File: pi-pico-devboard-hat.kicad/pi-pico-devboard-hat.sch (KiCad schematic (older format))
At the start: 12 parts, among them J1 Conn_01x24_Male, J2 Conn_Pico_1, J3 Conn_SWD, J4 Conn_Pico_2, P1 Conn_02x20_Odd_Even, SW1 SW_Reset, U1 Pico

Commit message: added footprints
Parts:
- D1: footprint (none) -> Diode_THT:D_DO-41_SOD81_P7.62mm_Horizontal
- J2, J4: footprint (none) -> Connector_PinHeader_2.54mm:PinHeader_1x20_P2.54mm_Vertical
- J3: footprint (none) -> Connector_PinHeader_2.54mm:PinHeader_1x03_P2.54mm_Vertical
- SW1: footprint (none) -> Button_Switch_THT:SW_PUSH_6mm
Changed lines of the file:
@@
 F 0 "J2" H 6400 5500 50  0000 C CNN
 F 1 "Conn_Pico_1" H 6400 5350 50  0000 C CNN
-F 2 "" H 6300 4300 50  0001 C CNN
+F 2 "Connector_PinHeader_2.54mm:PinHeader_1x20_P2.54mm_Vertical" H 6300 4300 50  0001 C CNN
 F 3 "~" H 6300 4300 50  0001 C CNN
 	1    6300 4300
@@
 F 0 "J4" H 9050 3050 50  0000 C CNN
 F 1 "Conn_Pico_2" H 9050 3200 50  0000 C CNN
-F 2 "" H 8900 4400 50  0001 C CNN
+F 2 "Connector_PinHeader_2.54mm:PinHeader_1x20_P2.54mm_Vertical" H 8900 4400 50  0001 C CNN
 F 3 "~" H 8900 4400 50  0001 C CNN
 	1    8900 4400
@@
 F 0 "J3" V 7754 6062 50  0000 R CNN
 F 1 "Conn_SWD" V 7663 6062 50  0000 R CNN
-F 2 "" H 7600 6250 50  0001 C CNN
+F 2 "Connector_PinHeader_2.54mm:PinHeader_1x03_P2.54mm_Vertical" H 7600 6250 50  0001 C CNN
 F 3 "~" H 7600 6250 50  0001 C CNN
 	1    7600 6250
@@
 F 0 "SW1" H 9400 4685 50  0000 C CNN
 F 1 "SW_Reset" H 9400 4594 50  0000 C CNN
-F 2 "" H 9400 4600 50  0001 C CNN
+F 2 "Button_Switch_THT:SW_PUSH_6mm" H 9400 4600 50  0001 C CNN
 F 3 "~" H 9400 4600 50  0001 C CNN
 	1    9400 4400
@@
 F 0 "D1" V 9846 2870 50  0000 R CNN
 F 1 "D_Schottky" V 9755 2870 50  0000 R CNN
-F 2 "" H 9800 2950 50  0001 C CNN
+F 2 "Diode_THT:D_DO-41_SOD81_P7.62mm_Horizontal" H 9800 2950 50  0001 C CNN
 F 3 "~" H 9800 2950 50  0001 C CNN
 	1    9800 2950

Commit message: updated footprint for pico
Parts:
- U1: footprint RPi_Pico:RPi_Pico_SMD_TH -> user:RPi_Pico_SMD_TH
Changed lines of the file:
@@
 F 0 "U1" H 7600 5565 50  0000 C CNN
 F 1 "Pico" H 7600 5474 50  0000 C CNN
-F 2 "RPi_Pico:RPi_Pico_SMD_TH" V 7600 4350 50  0001 C CNN
+F 2 "user:RPi_Pico_SMD_TH" V 7600 4350 50  0001 C CNN
 F 3 "" H 7600 4350 50  0001 C CNN
 	1    7600 4350

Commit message: Rev 2: removed unneeded connectors
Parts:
- removed J2: Conn_Pico_1, Connector_PinHeader_2.54mm:PinHeader_1x20_P2.54mm_Vertical, symbol Connector:Conn_01x20_Male
- removed J3: Conn_SWD, Connector_PinHeader_2.54mm:PinHeader_1x03_P2.54mm_Vertical, symbol Connector:Conn_01x03_Male
- removed J4: Conn_Pico_2, Connector_PinHeader_2.54mm:PinHeader_1x20_P2.54mm_Vertical, symbol Connector:Conn_01x20_Male
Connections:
- wire segments 147 -> 135
- no-connect marks 4 -> 28
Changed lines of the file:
@@
 Sheet 1 1
 Title "pi-pico-devboard-hat"
-Date "2021-03-11"
-Rev "1"
+Date "2021-03-18"
+Rev "2"
 Comp "Bernhard Bablok"
 Comment1 "https://github.com/bablokb/pi-pico-devboard-hat"
@@
 $EndComp
 $Comp
-L Connector:Conn_01x20_Male J2
-U 1 1 604A53BA
-P 6300 4300
-F 0 "J2" H 6400 5500 50  0000 C CNN
-F 1 "Conn_Pico_1" H 6400 5350 50  0000 C CNN
-F 2 "Connector_PinHeader_2.54mm:PinHeader_1x20_P2.54mm_Vertical" H 6300 4300 50  0001 C CNN
-F 3 "~" H 6300 4300 50  0001 C CNN
-	1    6300 4300
-	1    0    0    -1
-$EndComp
-$Comp
-L Connector:Conn_01x20_Male J4
-U 1 1 604AF8E6
-P 8900 4400
-F 0 "J4" H 9050 3050 50  0000 C CNN
-F 1 "Conn_Pico_2" H 9050 3200 50  0000 C CNN
-F 2 "Connector_PinHeader_2.54mm:PinHeader_1x20_P2.54mm_Vertical" H 8900 4400 50  0001 C CNN
-F 3 "~" H 8900 4400 50  0001 C CNN
-	1    8900 4400
-	-1   0    0    1
-$EndComp
-$Comp
-L Connector:Conn_01x03_Male J3
-U 1 1 604B1D35
-P 7600 6250
-F 0 "J3" V 7754 6062 50  0000 R CNN
-F 1 "Conn_SWD" V 7663 6062 50  0000 R CNN
-F 2 "Connector_PinHeader_2.54mm:PinHeader_1x03_P2.54mm_Vertical" H 7600 6250 50  0001 C CNN
-F 3 "~" H 7600 6250 50  0001 C CNN
-	1    7600 6250
-	0    -1   -1   0
-$EndComp
-$Comp
 L Switch:SW_Push SW1
 U 1 1 604B3ACB
@@
 $EndComp
 Wire Wire Line
-	8300 3500 8700 3500
-Wire Wire Line
-	8300 3600 8700 3600
-Wire Wire Line
-	8300 3700 8700 3700
-Wire Wire Line
-	8300 3800 8700 3800
-Wire Wire Line
-	8300 3900 8700 3900
-Wire Wire Line
 	8300 4000 8700 4000
 Wire Wire Line
-	8300 4100 8700 4100
-Wire Wire Line
 	8300 4200 8700 4200
 Wire Wire Line
 	8300 4300 8700 4300
 Wire Wire Line
-	8300 4400 8700 4400
-Wire Wire Line
 	8300 4500 8700 4500
 Wire Wire Line
-	8300 4600 8700 4600
-Wire Wire Line
 	8300 4700 8700 4700
 Wire Wire Line
@@
 	8300 5000 8700 5000
 Wire Wire Line
-	8300 5100 8700 5100
-Wire Wire Line
 	8300 5200 8700 5200
 Wire Wire Line
 	8300 5300 8700 5300
 Wire Wire Line
-	6500 3400 6850 3400
-Wire Wire Line
-	6500 3500 6750 3500
-Wire Wire Line
-	6500 3600 6900 3600
-Wire Wire Line
 	6500 3700 6900 3700
 Wire Wire Line
@@
 	6500 4000 6900 4000
 Wire Wire Line
-	6500 4100 6900 4100
-Wire Wire Line
 	6500 4200 6900 4200
 Wire Wire Line
@@
 Wire Wire Line
 	6500 4500 6900 4500
-Wire Wire Line
-	6500 4600 6900 4600
-Wire Wire Line
-	6500 4700 6900 4700
-Wire Wire Line
-	6500 4800 6900 4800
-Wire Wire Line
-	6500 4900 6900 4900
-Wire Wire Line
-	6500 5000 6900 5000
-Wire Wire Line
-	6500 5100 6900 5100
-Wire Wire Line
-	6500 5200 6900 5200
-Wire Wire Line
-	6500 5300 6900 5300
-Wire Wire Line
-	8700 4400 9200 4400
-Connection ~ 8700 4400
 $Comp
 L power:GND #PWR07
@@
 	9600 4400 9800 4400
 Wire Wire Line
-	8700 3600 9800 3600
-Wire Wire Line
 	9800 3600 9800 4400
-Connection ~ 8700 3600
 Wire Wire Line
 	9800 4600 9800 4400
-Connection ~ 8700 4600
 Connection ~ 9800 4400
 Connection ~ 9800 4600
 Wire Wire Line
-	8700 4600 9800 4600
-Wire Wire Line
 	9800 4600 9800 5100
-Wire Wire Line
-	9800 5100 8700 5100
-Connection ~ 8700 5100
 $Comp
 L power:GND #PWR05
@@
 $EndComp
 Wire Wire Line
-	6500 3600 5950 3600
-Wire Wire Line
 	5950 3600 5950 4100
-Connection ~ 6500 3600
 Connection ~ 5950 4100
 Wire Wire Line
@@
 Wire Wire Line
 	5950 4100 5950 4600
-Wire Wire Line
-	5950 4600 6500 4600
-Connection ~ 6500 4600
-Wire Wire Line
-	6500 5100 5950 5100
-Connection ~ 6500 5100
 Connection ~ 5950 4600
 $Comp
@@
 	0    -1   -1   0
 $EndComp
-Connection ~ 8700 3500
 $Comp
 L power:PWR_FLAG #FLG0101
@@
 	7600 5650 7600 5500
 Connection ~ 9800 5100
-Wire Wire Line
-	6500 4100 5950 4100
-Connection ~ 6500 4100
 NoConn ~ 2400 2400
 NoConn ~ 2900 2400
@@
 $EndComp
 Connection ~ 2200 950
-Wire Wire Line
-	8300 3400 8700 3400
 Text Label 10300 3400 2    50   ~ 0
 VBUS
@@
 Wire Wire Line
 	10300 3400 10500 3400
-Text Label 8350 3400 0    50   ~ 0
-VBUS
 Text Label 10300 3700 2    50   ~ 0
 3V3_EN
@@
 Wire Wire Line
 	9800 3100 9800 3500
-Wire Wire Line
-	8700 3500 9800 3500
 Text Label 10300 3500 2    50   ~ 0
 VSYS
@@
 Text Label 7700 5900 0    50   ~ 0
 GPIO24(GEN5)
-Wire Wire Line
-	7700 5500 7700 6050
-Wire Wire Line
-	7600 5650 7600 6050
 Text Label 7500 5900 2    50   ~ 0
 GPIO25(GEN6)
-Wire Wire Line
-	7500 5500 7500 6050
 Text Label 6850 3100 0    50   ~ 0
 GPIO15(RXD0)
@@
 Wire Wire Line
 	6850 3100 6850 3400
-Connection ~ 6850 3400
 Wire Wire Line
 	6850 3400 6900 3400
 Wire Wire Line
 	6750 3000 6750 3500
-Connection ~ 6750 3500
 Wire Wire Line
 	6750 3500 6900 3500
+Wire Wire Line
+	5950 4600 6900 4600
+Wire Wire Line
+	5950 5100 6900 5100
+Wire Wire Line
+	5950 3600 6900 3600
+Wire Wire Line
+	5950 4100 6900 4100
+Wire Wire Line
+	6500 4700 6900 4700
+Wire Wire Line
+	6500 4800 6900 4800
+Wire Wire Line
+	6500 4900 6900 4900
+Wire Wire Line
+	6500 5000 6900 5000
+Wire Wire Line
+	6500 5200 6900 5200
+Wire Wire Line
+	6500 5300 6900 5300
+Wire Wire Line
+	8300 4400 9200 4400
+Wire Wire Line
+	8300 3600 9800 3600
+Wire Wire Line
+	8300 3500 9800 3500
+Wire Wire Line
+	8300 5100 9800 5100
+Wire Wire Line
+	8300 4600 9800 4600
+Text Label 8350 3400 0    50   ~ 0
+VBUS
+Wire Wire Line
+	8300 3400 8350 3400
+Wire Wire Line
+	8300 3700 8350 3700
+Wire Wire Line
+	8300 3800 8350 3800
+Wire Wire Line
+	8300 3900 8350 3900
+Wire Wire Line
+	8300 4100 8350 4100
+NoConn ~ 6500 3700
+NoConn ~ 6500 3800
+NoConn ~ 6500 3900
+NoConn ~ 6500 4000
+NoConn ~ 6500 4200
+NoConn ~ 6500 4300
+NoConn ~ 6500 4400
+NoConn ~ 6500 4500
+NoConn ~ 6500 4700
+NoConn ~ 6500 4800
+NoConn ~ 6500 4900
+NoConn ~ 6500 5000
+NoConn ~ 6500 5200
+NoConn ~ 6500 5300
+NoConn ~ 8700 4000
+NoConn ~ 8700 4200
+NoConn ~ 8700 4300
+NoConn ~ 8700 4500
+NoConn ~ 8700 4700
+NoConn ~ 8700 4800
+NoConn ~ 8700 4900
+NoConn ~ 8700 5000
+NoConn ~ 8700 5200
+NoConn ~ 8700 5300
+Wire Wire Line
+	7700 5500 7700 5900
+Wire Wire Line
+	7500 5500 7500 5900
 $EndSCHEMATC

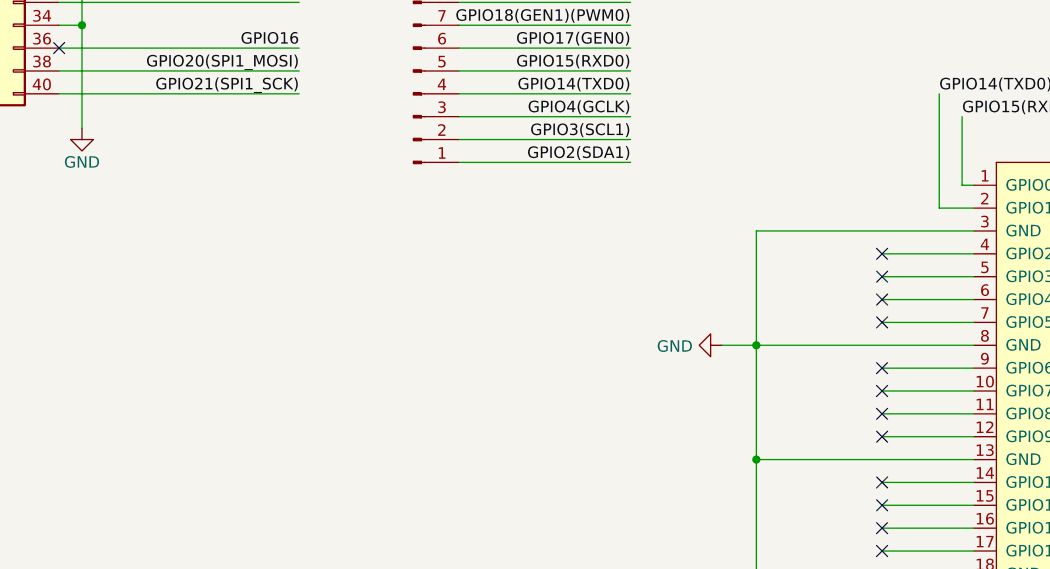
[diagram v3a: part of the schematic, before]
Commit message: Rev 3: added IC-connector with optional pullups
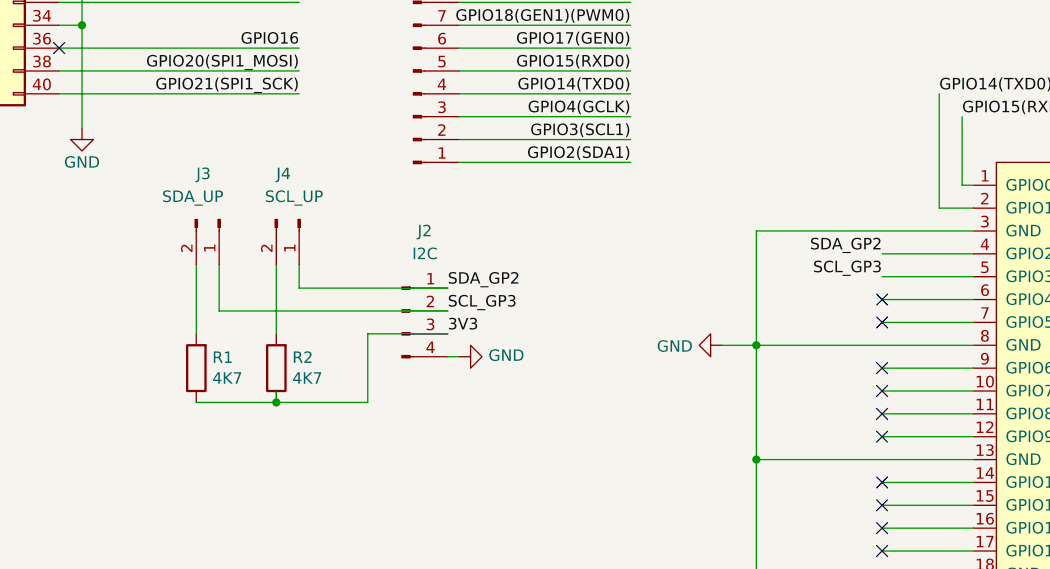
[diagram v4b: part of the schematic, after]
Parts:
- added J2: I2C, Connector_PinHeader_2.54mm:PinHeader_1x04_P2.54mm_Vertical, symbol Connector:Conn_01x04_Male
- added J3: SDA_UP, Connector_PinHeader_2.54mm:PinHeader_1x02_P2.54mm_Vertical, symbol Connector:Conn_01x02_Male
- added J4: SCL_UP, Connector_PinHeader_2.54mm:PinHeader_1x02_P2.54mm_Vertical, symbol Connector:Conn_01x02_Male
- added R1, R2: 4K7, Resistor_THT:R_Axial_DIN0207_L6.3mm_D2.5mm_P7.62mm_Horizontal, symbol Device:R
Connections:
- net 3V3: now also J2.3 (Pin_3), R1.1, R2.1
- net GND: now also J2.4 (Pin_4)
- net SDA_GP2: now reaches U1.4 (GPIO2)
- net SDA_GP2: now also J2.1 (Pin_1), J4.1 (Pin_1)
- net SCL_GP3: now reaches U1.5 (GPIO3)
- net SCL_GP3: now also J2.2 (Pin_2), J3.1 (Pin_1)
- new net: J4.2 (Pin_2), R2.2
- new net: J3.2 (Pin_2), R1.2
- no-connect marks 28 -> 26
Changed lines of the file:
@@
 Title "pi-pico-devboard-hat"
 Date "2021-03-18"
-Rev "2"
+Rev "3"
 Comp "Bernhard Bablok"
 Comment1 "https://github.com/bablokb/pi-pico-devboard-hat"
@@
 Wire Wire Line
 	8300 4100 8350 4100
-NoConn ~ 6500 3700
-NoConn ~ 6500 3800
 NoConn ~ 6500 3900
 NoConn ~ 6500 4000
@@
 Wire Wire Line
 	7500 5500 7500 5900
+$Comp
+L Connector:Conn_01x04_Male J2
+U 1 1 6061A256
+P 4400 3950
+F 0 "J2" H 4500 4300 50  0000 C CNN
+F 1 "I2C" H 4500 4200 50  0000 C CNN
+F 2 "Connector_PinHeader_2.54mm:PinHeader_1x04_P2.54mm_Vertical" H 4400 3950 50  0001 C CNN
+F 3 "~" H 4400 3950 50  0001 C CNN
+	1    4400 3950
+	1    0    0    -1
+$EndComp
+Text Label 4600 3850 0    50   ~ 0
+SDA_GP2
+Text Label 6500 3700 2    50   ~ 0
+SDA_GP2
+Text Label 4600 3950 0    50   ~ 0
+SCL_GP3
+Text Label 6500 3800 2    50   ~ 0
+SCL_GP3
+Text Label 4600 4050 0    50   ~ 0
+3V3
+$Comp
+L power:GND #PWR0101
+U 1 1 6061BF4A
+P 4650 4150
+F 0 "#PWR0101" H 4650 3900 50  0001 C CNN
+F 1 "GND" V 4655 4022 50  0000 R CNN
+F 2 "" H 4650 4150 50  0001 C CNN
+F 3 "" H 4650 4150 50  0001 C CNN
+	1    4650 4150
+	0    -1   -1   0
+$EndComp
+Wire Wire Line
+	4600 4150 4650 4150
+$Comp
+L Device:R R2
+U 1 1 6062584D
+P 3850 4200
+F 0 "R2" H 3780 4154 50  0000 R CNN
+F 1 "4K7" H 3780 4245 50  0000 R CNN
+F 2 "Resistor_THT:R_Axial_DIN0207_L6.3mm_D2.5mm_P7.62mm_Horizontal" V 3780 4200 50  0001 C CNN
+F 3 "~" H 3850 4200 50  0001 C CNN
+	1    3850 4200
+	-1   0    0    1
+$EndComp
+$Comp
+L Device:R R1
+U 1 1 60626297
+P 3500 4200
+F 0 "R1" H 3430 4154 50  0000 R CNN
+F 1 "4K7" H 3430 4245 50  0000 R CNN
+F 2 "Resistor_THT:R_Axial_DIN0207_L6.3mm_D2.5mm_P7.62mm_Horizontal" V 3430 4200 50  0001 C CNN
+F 3 "~" H 3500 4200 50  0001 C CNN
+	1    3500 4200
+	-1   0    0    1
+$EndComp
+$Comp
+L Connector:Conn_01x02_Male J3
+U 1 1 60626EA3
+P 3600 3550
+F 0 "J3" V 3400 3450 50  0000 L CNN
+F 1 "SDA_UP" V 3500 3300 50  0000 L CNN
+F 2 "Connector_PinHeader_2.54mm:PinHeader_1x02_P2.54mm_Vertical" H 3600 3550 50  0001 C CNN
+F 3 "~" H 3600 3550 50  0001 C CNN
+	1    3600 3550
+	0    1    1    0
+$EndComp
+$Comp
+L Connector:Conn_01x02_Male J4
+U 1 1 606291D7
+P 3950 3550
+F 0 "J4" V 3750 3450 50  0000 L CNN
+F 1 "SCL_UP" V 3850 3400 50  0000 L CNN
+F 2 "Connector_PinHeader_2.54mm:PinHeader_1x02_P2.54mm_Vertical" H 3950 3550 50  0001 C CNN
+F 3 "~" H 3950 3550 50  0001 C CNN
+	1    3950 3550
+	0    1    1    0
+$EndComp
+Wire Wire Line
+	4600 3850 3950 3850
+Wire Wire Line
+	3950 3850 3950 3750
+Wire Wire Line
+	4600 3950 3600 3950
+Wire Wire Line
+	3600 3950 3600 3750
+Wire Wire Line
+	3500 3750 3500 4050
+Wire Wire Line
+	3850 3750 3850 4050
+Wire Wire Line
+	4600 4050 4250 4050
+Wire Wire Line
+	4250 4050 4250 4350
+Wire Wire Line
+	4250 4350 3850 4350
+Wire Wire Line
+	3850 4300 3850 4350
+Wire Wire Line
+	3850 4350 3500 4350
+Connection ~ 3850 4350
 $EndSCHEMATC
